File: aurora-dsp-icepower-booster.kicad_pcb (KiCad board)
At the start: 2 copper layers, 200 x 200 mm, 243 parts, among them J1 XLR_IN_1, J10 XLR3_OUT, J11 XLR3_OUT, J12 XLR3_OUT, J13 24V DC, J14 REMOTE 3.5mm, J2 XLR_IN_2, J3 XLR_IN_3, J4 XLR_IN_4, J5 XLR_IN_5, J6 XLR_IN_6, J7 XLR3_OUT, J8 XLR3_OUT, J9 XLR3_OUT, SW1 Gain CH1, SW2 Gain CH2, SW3 Gain CH3, SW4 Gain CH4, SW5 Gain CH5, SW6 Gain CH6, SW7 ALWAYS/REMOTE, U1 LM4562, U10 LM4562, U11 LM4562, U12 LM4562, U13 TEL5-2422, U14 ADP7118ARDZ-11, U15 ADP7182AUJZ-11, U2 LM4562, U3 LM4562, U4 LM4562, U5 LM4562, U6 LM4562, U7 LM4562, U8 LM4562, U9 LM4562

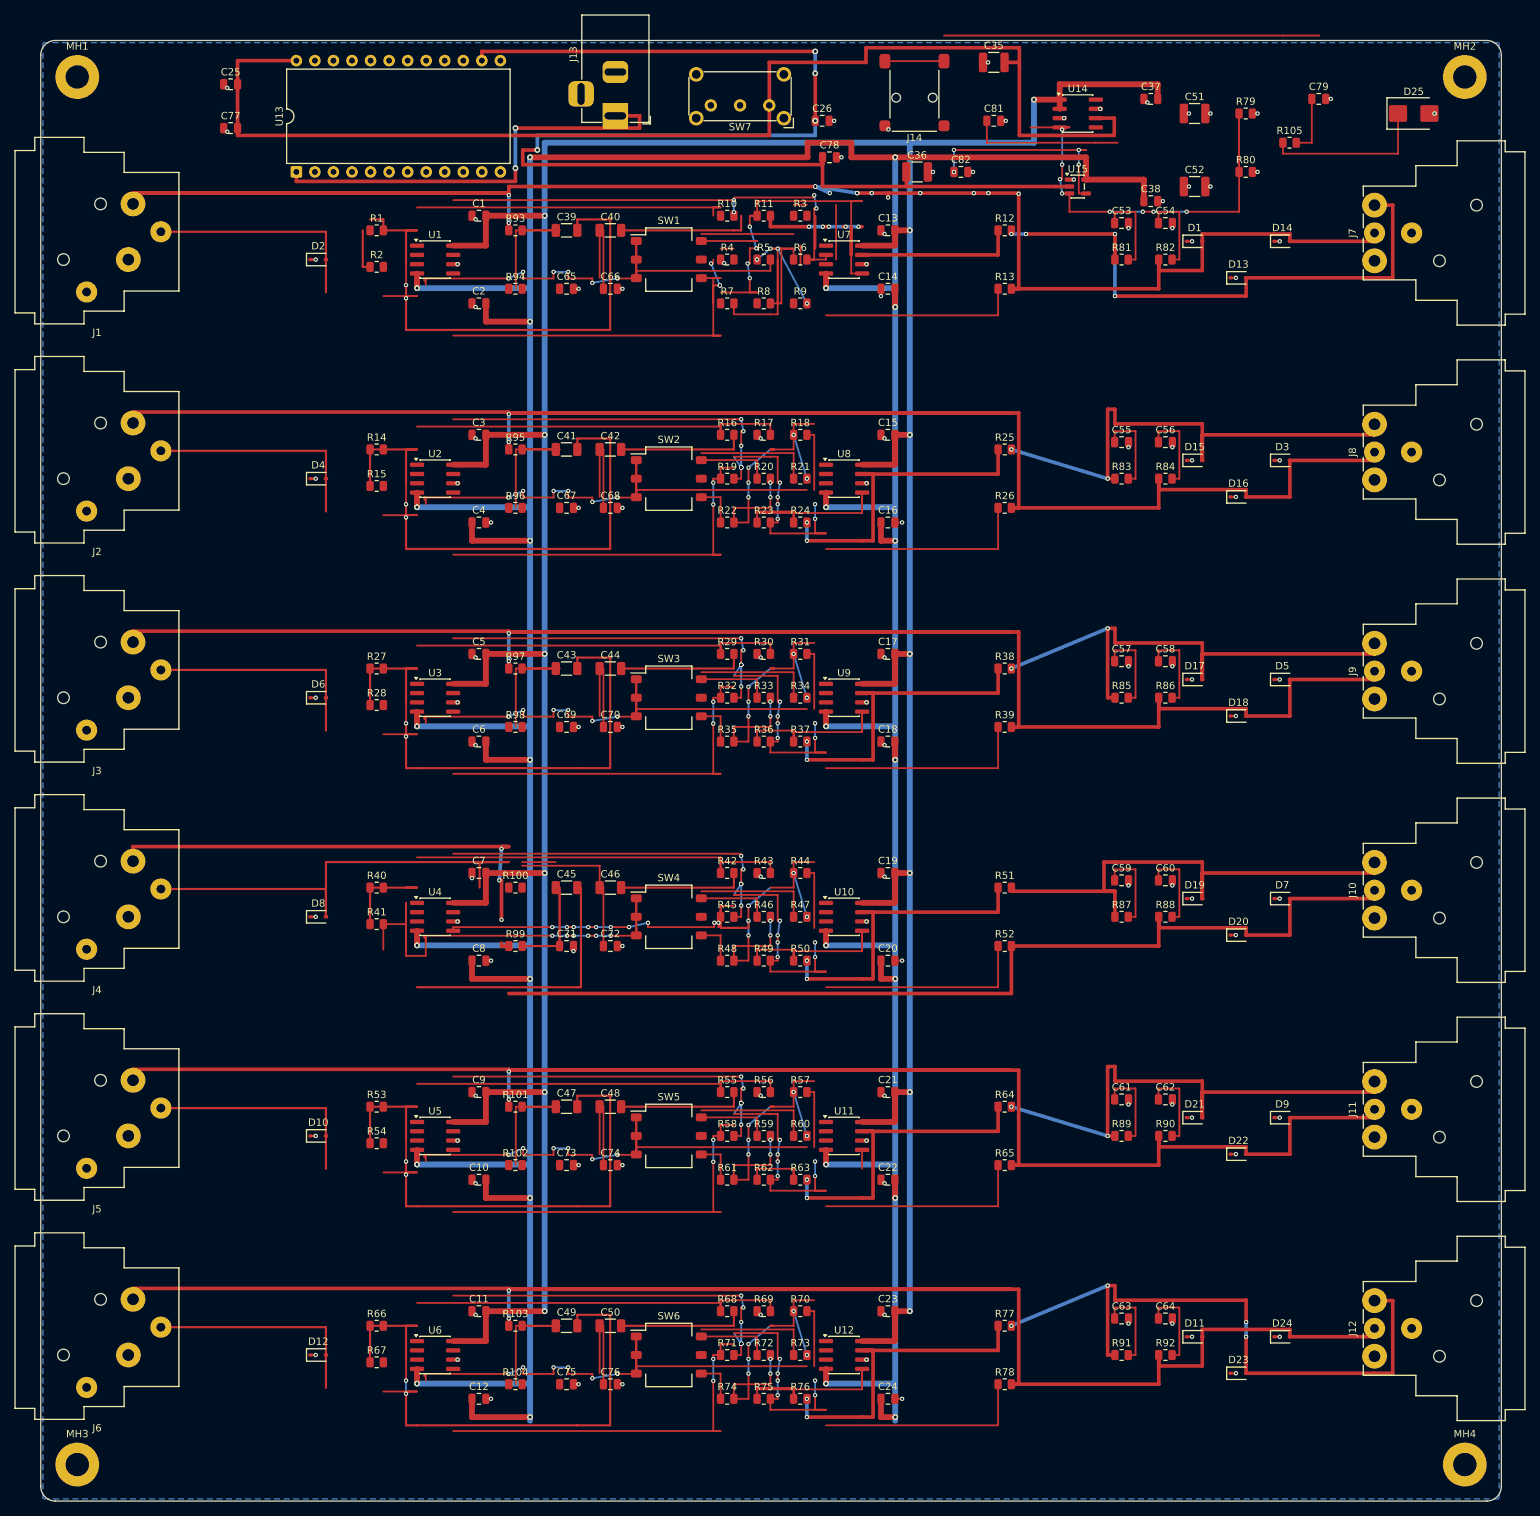
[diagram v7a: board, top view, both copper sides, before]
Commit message: Phase 6a: 275 dangling stubs entfernt, 0 DRC errors
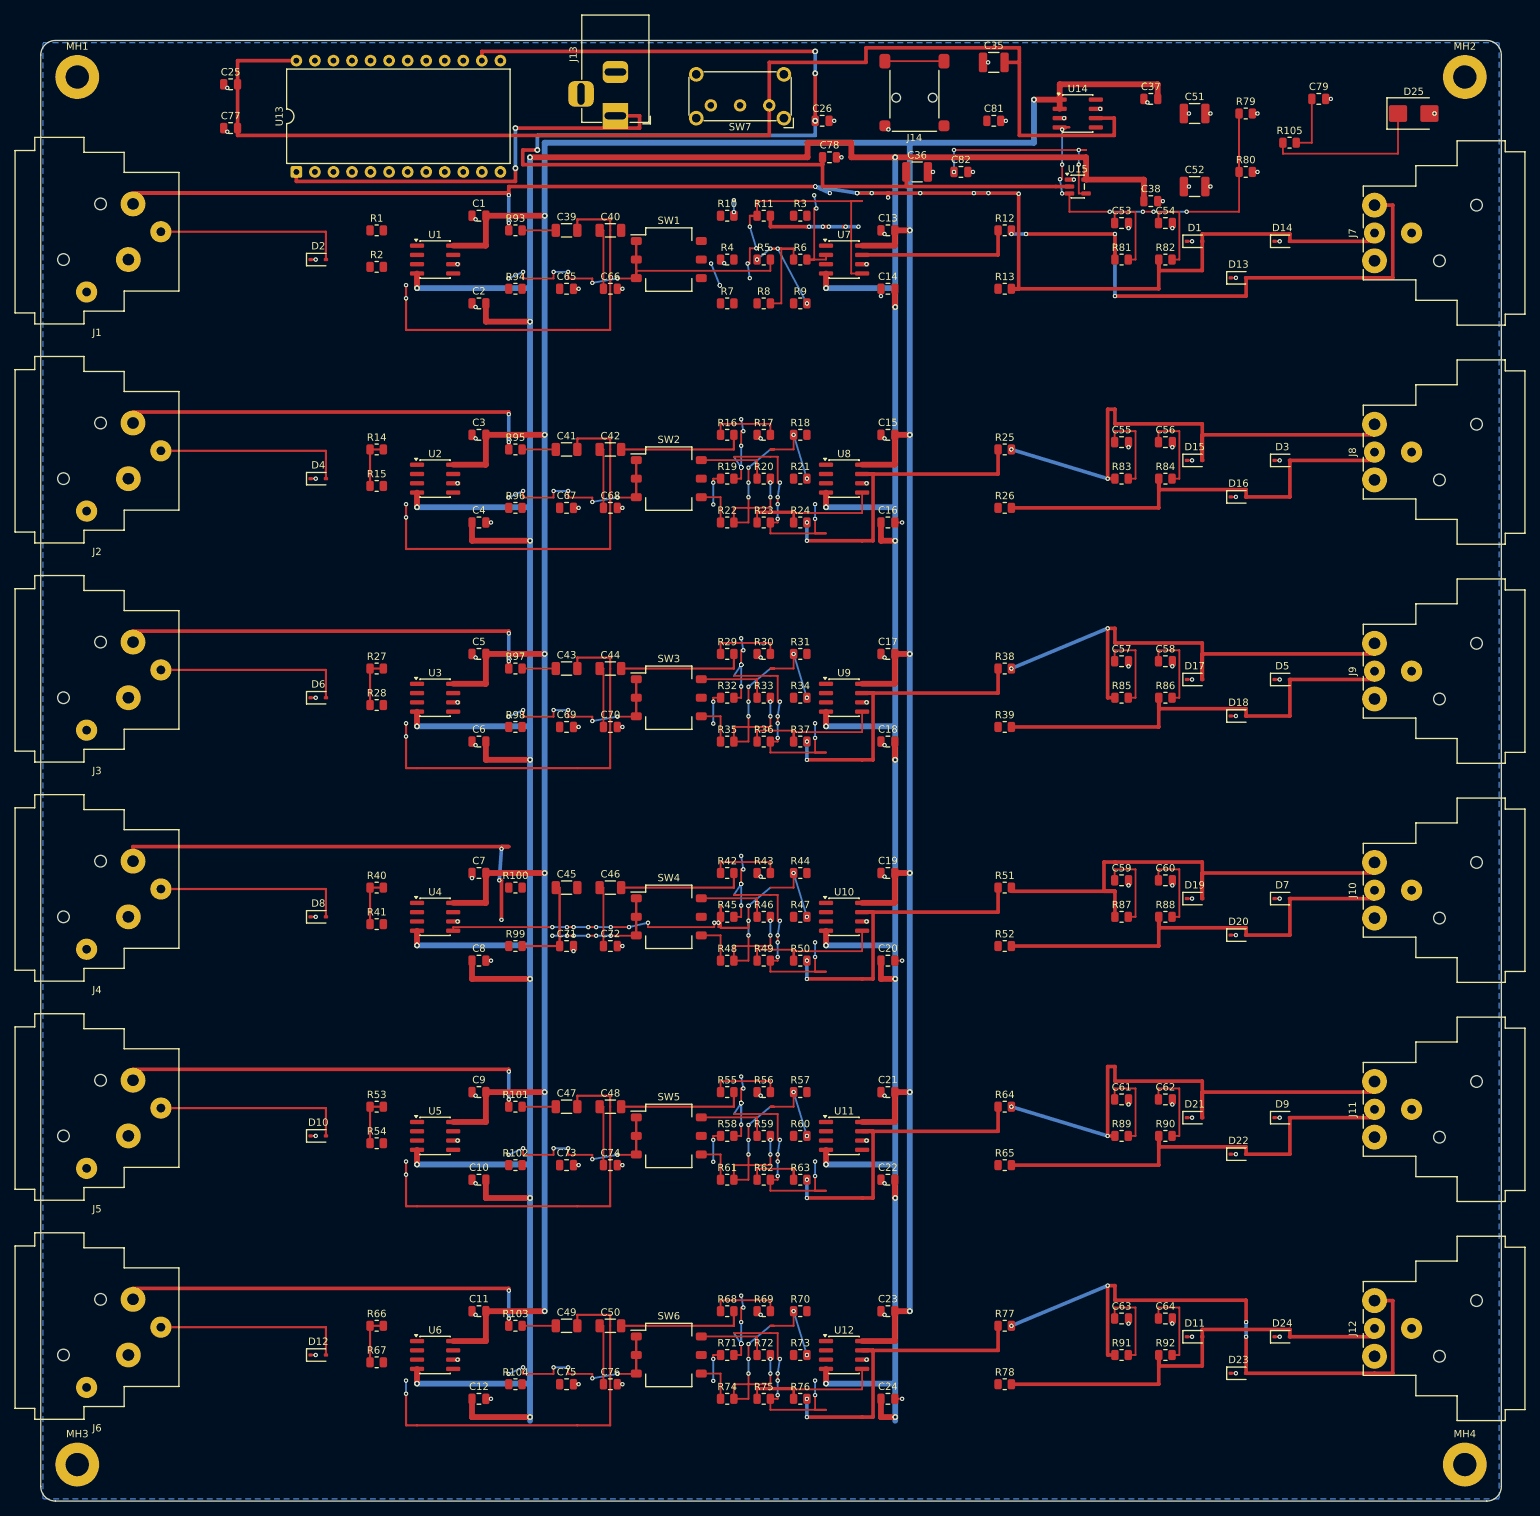
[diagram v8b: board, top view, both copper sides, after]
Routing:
- net /CH6_OUT_COLD: track 273.1 -> 120.4 mm
- net /CH5_OUT_COLD: track 273.1 -> 120.4 mm
- net /CH3_OUT_COLD: track 273.1 -> 120.4 mm
- net /CH2_OUT_COLD: track 273.1 -> 120.4 mm
- net /CH4_OUT_COLD: track 203.9 -> 127.2 mm
- net /CH4_RX_OUT: track 78.6 -> 21.7 mm
- net /CH1_GAIN_OUT: track 69.8 -> 15.5 mm
- net /CH1_SW_OUT_3: track 56.6 -> 3.23 mm
- net /CH6_SUMNODE: track 94.5 -> 42.4 mm
- net /CH5_SUMNODE: track 94.0 -> 41.9 mm
- net /CH3_SUMNODE: track 94.5 -> 42.4 mm
- net /CH2_SUMNODE: track 94.0 -> 41.9 mm
- net /REMOTE_IN: track 82.3 -> 30.9 mm
- net /CH3_RX_OUT: track 76.9 -> 31.3 mm
- net /CH2_RX_OUT: track 76.9 -> 31.3 mm
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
